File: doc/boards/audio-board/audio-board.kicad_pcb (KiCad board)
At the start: 2 copper layers, 173 x 85 mm, 268 parts, among them IC10 NE5532, IC11 NE5532, IC12 NE5532, IC13 MK2703B, IC14 CS4272, IC15 NE5532, IC16 NE5532, IC17 NE5532, IC3 LM7805CT, IC4 L4931CZ33, IC5 INA103, IC6 NE5532, IC7 NE5532, IC8 NE5532, IC9 INA103, P10 IN1SWB, P11 IN2SWB, P14 IN1G, P15 IN2G, P16 OUT1ASYM, P17 OUT2ASYM, P18 OUT1XLR, P19 OUT2XLR, P2 CONN_01X03, P3 CONN_01X10, P4 IN1XLR, P5 IN2XLR, P6 IN1TRS, P7 IN2TRS, P8 IN1SWA, P9 IN2SWA, Q1 BC639, Q2 BC640, Q3 BC547B, Y1 27M

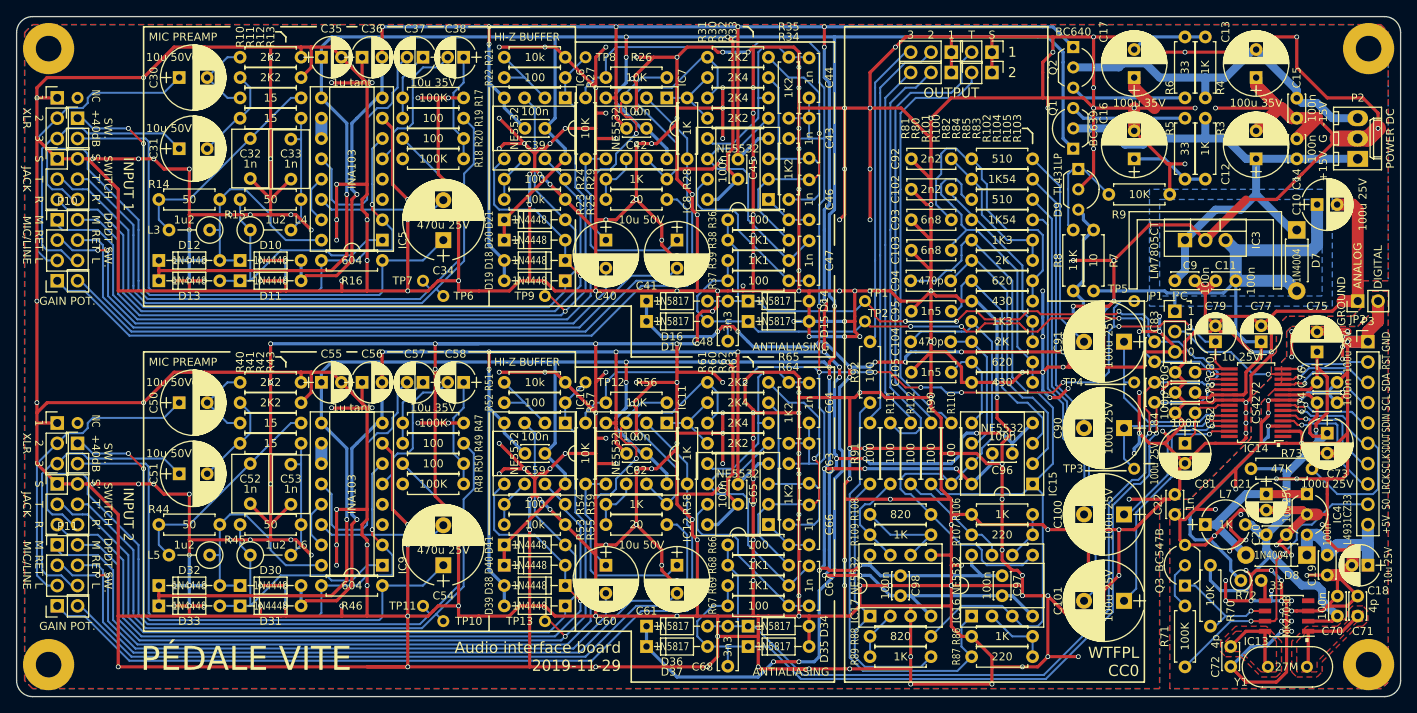
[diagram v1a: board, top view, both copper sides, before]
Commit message: Updated board files to KiCAD 6
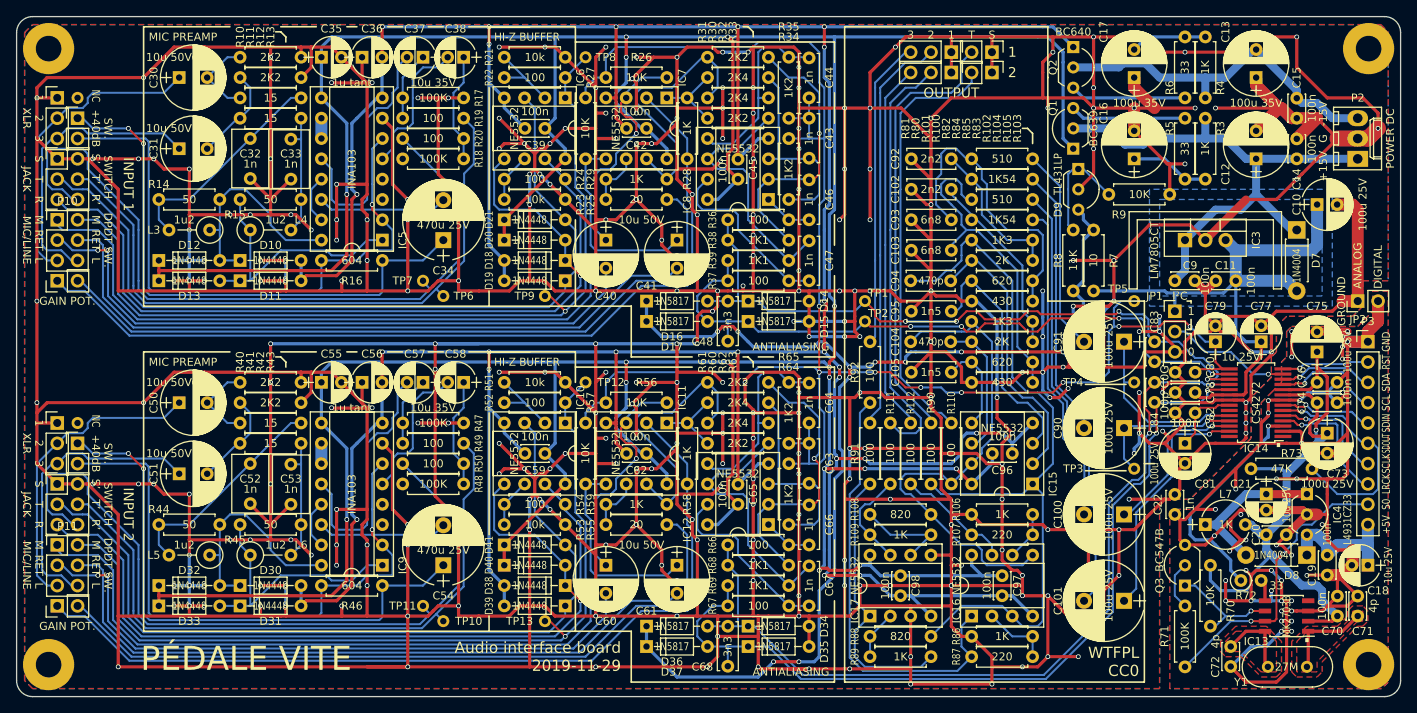
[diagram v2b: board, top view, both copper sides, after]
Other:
- net class Default removed
- net class Larger removed
- net class Power removed
- net class Power2 removed
- net class Power3 removed
- board text added: "~{RST}"
- board text removed: "~RST"
